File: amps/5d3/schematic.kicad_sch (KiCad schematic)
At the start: 43 parts, among them T2 PP : 8

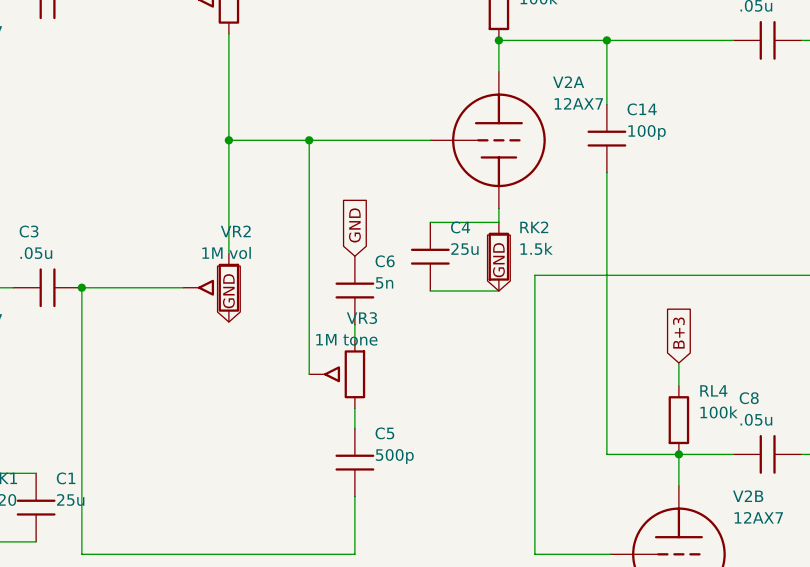
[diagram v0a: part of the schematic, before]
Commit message: Fix: one lettering convention per surface, engine-enforced; legend inside the viewBox
WS3 — layout pipeline + cross-surface value-consistency engine.

## One convention per surface (docs/lettering-conventions.md, new)

The same part stated its value in several notations at once. 5E3 C6 and 5D3 C6
rendered "5n" on the schematic, "0.005 µF · 600 V" in the parts list and
"0.005 µF" on the board. 5F6-A RD1 printed "4,700 Ω" beside neighbours printing
"15 kΩ". check_value_consistency proves the surfaces name the same QUANTITY; it
cannot see that they name it three ways. So each surface now has exactly one
convention and every one of them is gated:

* house units in bom.yaml/prose — engineering prefix with the mantissa 1…999,
  pF below 1000 pF and µF at and above it, no comma-grouped thousands. 19 values
  normalised (5E6-A, 5F6-A, 5F10, 6161, 6G2, 6G5, 6G6-B).
* schematic drafting shorthand — the unit letter is the SI prefix of the house
  unit, in the amp's declared idiom (meta.yaml conventions.notation: us|uk).
  British RKM/nanofarad practice on the Hiwatt and the 2204 is DECLARED, not
  normalised away; it is what those source drawings letter. Secondary ratings
  are space-separated fields with their own unit ("20u 600V"), never the era's
  dashed shorthand and never the house middot. 30 symbol values corrected across
  ten draw scripts.
* era sheet lettering — generated only, by era_pair(); documented cases and a
  corpus round-trip sweep in test_era_values.py, now 57 cases.

## Era-lettering fall-throughs closed

A value era_pair() refuses came back as the house string, and a house string can
be a whole sentence. Fixed at the source rather than per case:

* body_value() — a parenthetical GLOSS is never lettered on a component body.
  "selenium (silicon diode in modern builds)" was lettered in full on the 5E4-A
  and ran off the left edge of the page.
* twin cans letter as the era sheets did: 25 µF + 25 µF -> "25/25MFD".
* a repeat count is not a rating: "(×2)" com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
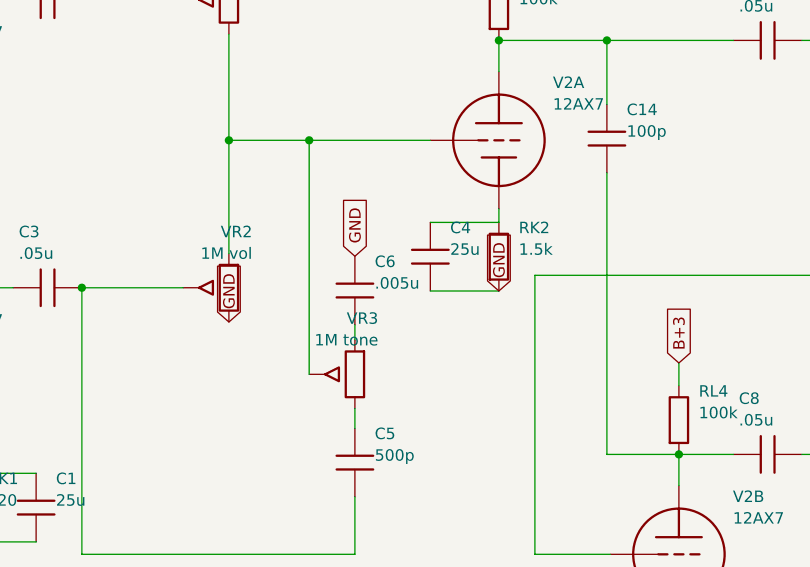
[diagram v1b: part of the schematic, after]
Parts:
- C6: value 5n -> .005u
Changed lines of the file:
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@@
     (in_bom yes) (on_board yes)
     (property "Reference" "C6" (at 106.2 117.49 0) (effects (font (size 1.27 1.27)) (justify left)))
-    (property "Value" "5n" (at 106.2 119.89 0) (effects (font (size 1.27 1.27)) (justify left))))
+    (property "Value" ".005u" (at 106.2 119.89 0) (effects (font (size 1.27 1.27)) (justify left))))
   (global_label "GND" (shape input) (at 104 116.88 270)
     (effects (font (size 1.27 1.27)) (justify left)))

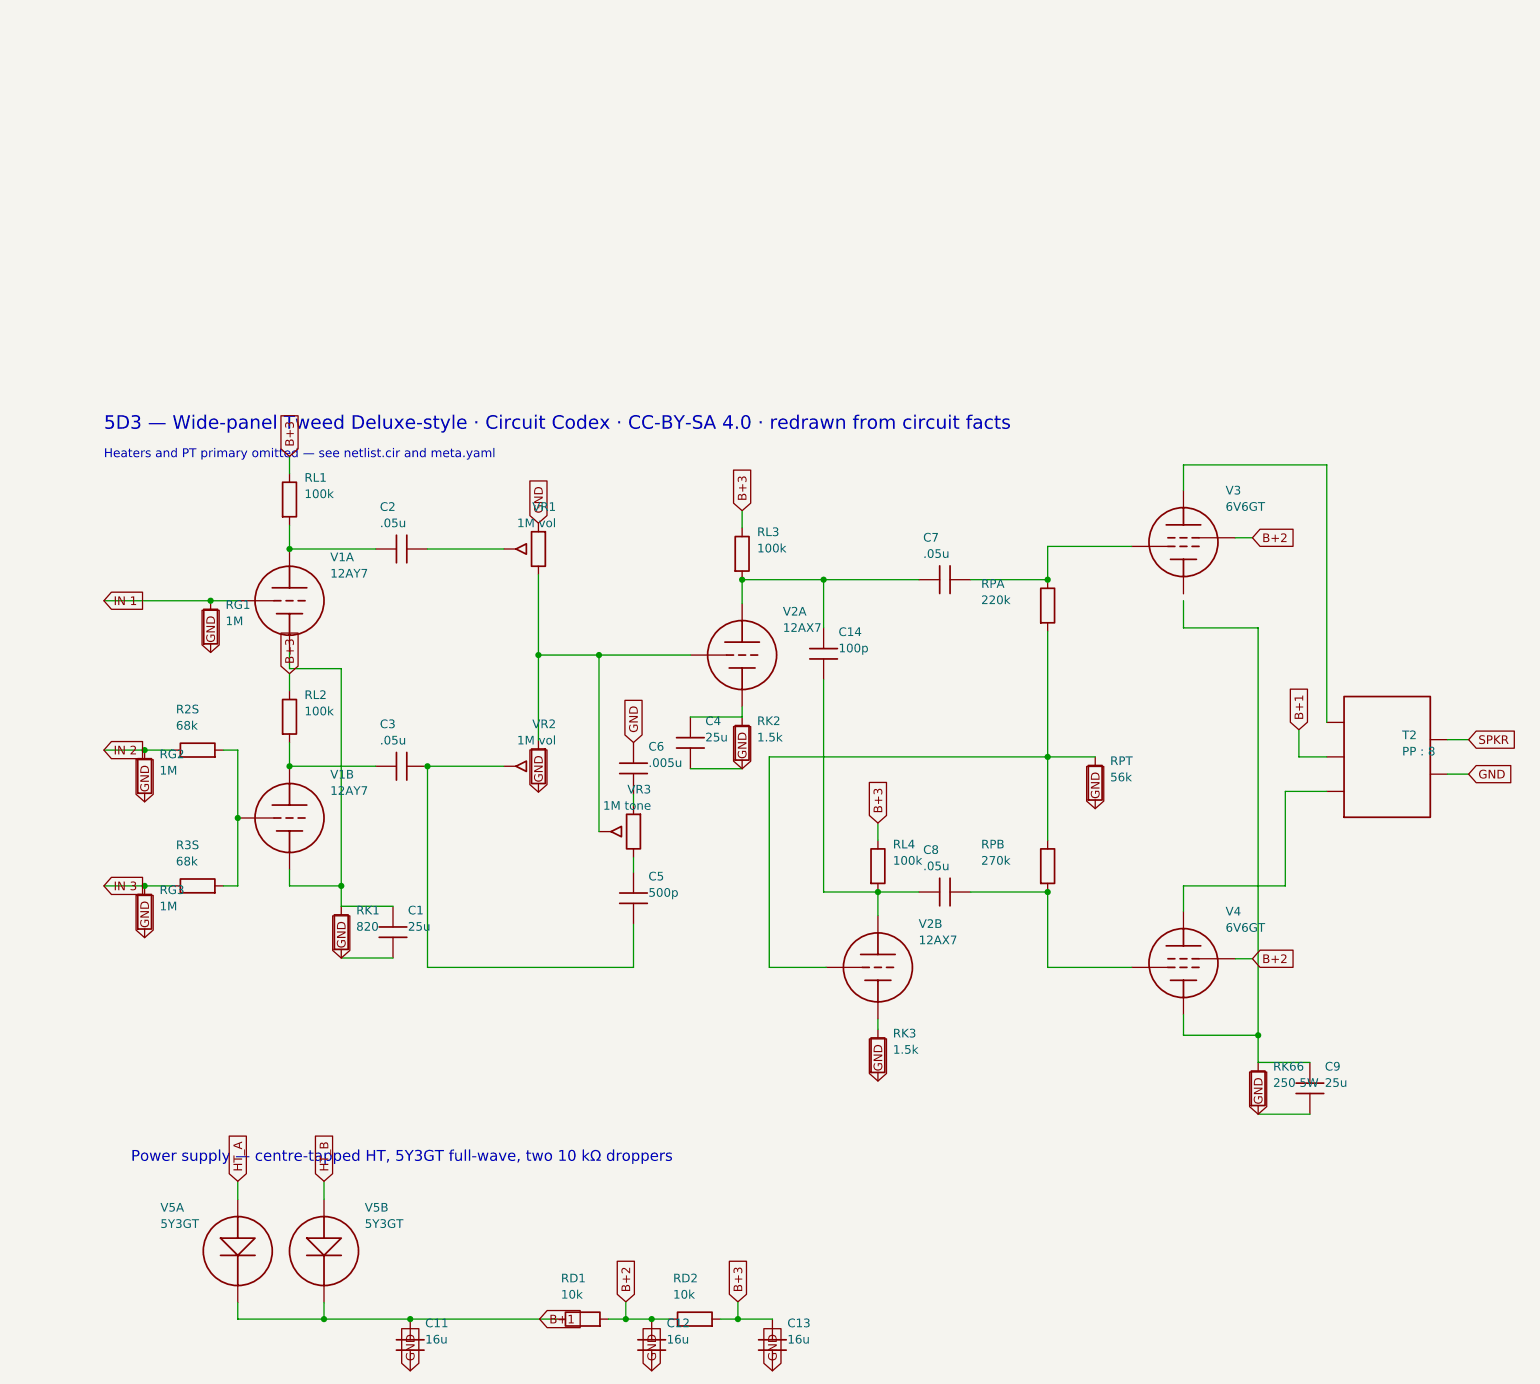
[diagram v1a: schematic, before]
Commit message: Update: regenerate every drawing the four merged units changed
The four parallel units all rewrote generators, so their committed artifacts
were each generated against only their own third of the merged pipeline. Every
schematic, both layout styles, the social cards and the manifest are rebuilt
here from the merged sources, so what ships is what the merged generators draw.

One integration fault the rebuild exposed, invisible to any single unit:

- 5E5-A: the note explaining that the Presence wiper and the 100k feedback
  resistor land on V3A's GRID (not its cathode, as on the 5F4) was added as a
  hand-placed `s.text()` at a coordinate chosen before the sheet gained a
  reserved notes band. Merged, it printed through the -32V bias label. Moved to
  `note()`, which wraps prose into that band — the exact failure mode the band
  was built to end.

Three conflicts resolved against docs/lettering-conventions.md rather than by
picking a side, since two units had corrected the same lines for different
reasons:

- 5E5-A tone/feedback caps take the corrected designators (C7, C8, C9, RNF —
  `C_tr1`/`C_NFB` were generator identifiers that had leaked onto a published
  board) with the house-derived lettering (`.01u 400V`, `500p`, `.1u 200V`).
  Dropping the working voltage or writing `.0005u` would have lost a rating the
  source prints and re-broken the pF/µF decade rule.
- 5D3 C6 and 6G6-B's three cathode resistors take the SI-prefix form the
  convention binds (`.005u`, `2.7k`, `1.5k`), keeping the ground-flag direction
  fix and the removal of the second `gnd()` that shorted each cathode it biased.
- 5F6-A's bias supply keeps both 8 µF cans drawn — the second was previously a
  parenthetical claiming one of two was shown — at the coordinates that clear
  the title-block strip.

All gates green, including check_value_consistency at zero disagreements.

🤖 Generated with [Claude Code](https://claude.com/claude-code)

Co-Authored-By: Claude Fable 5 <noreply@anthropic.com>
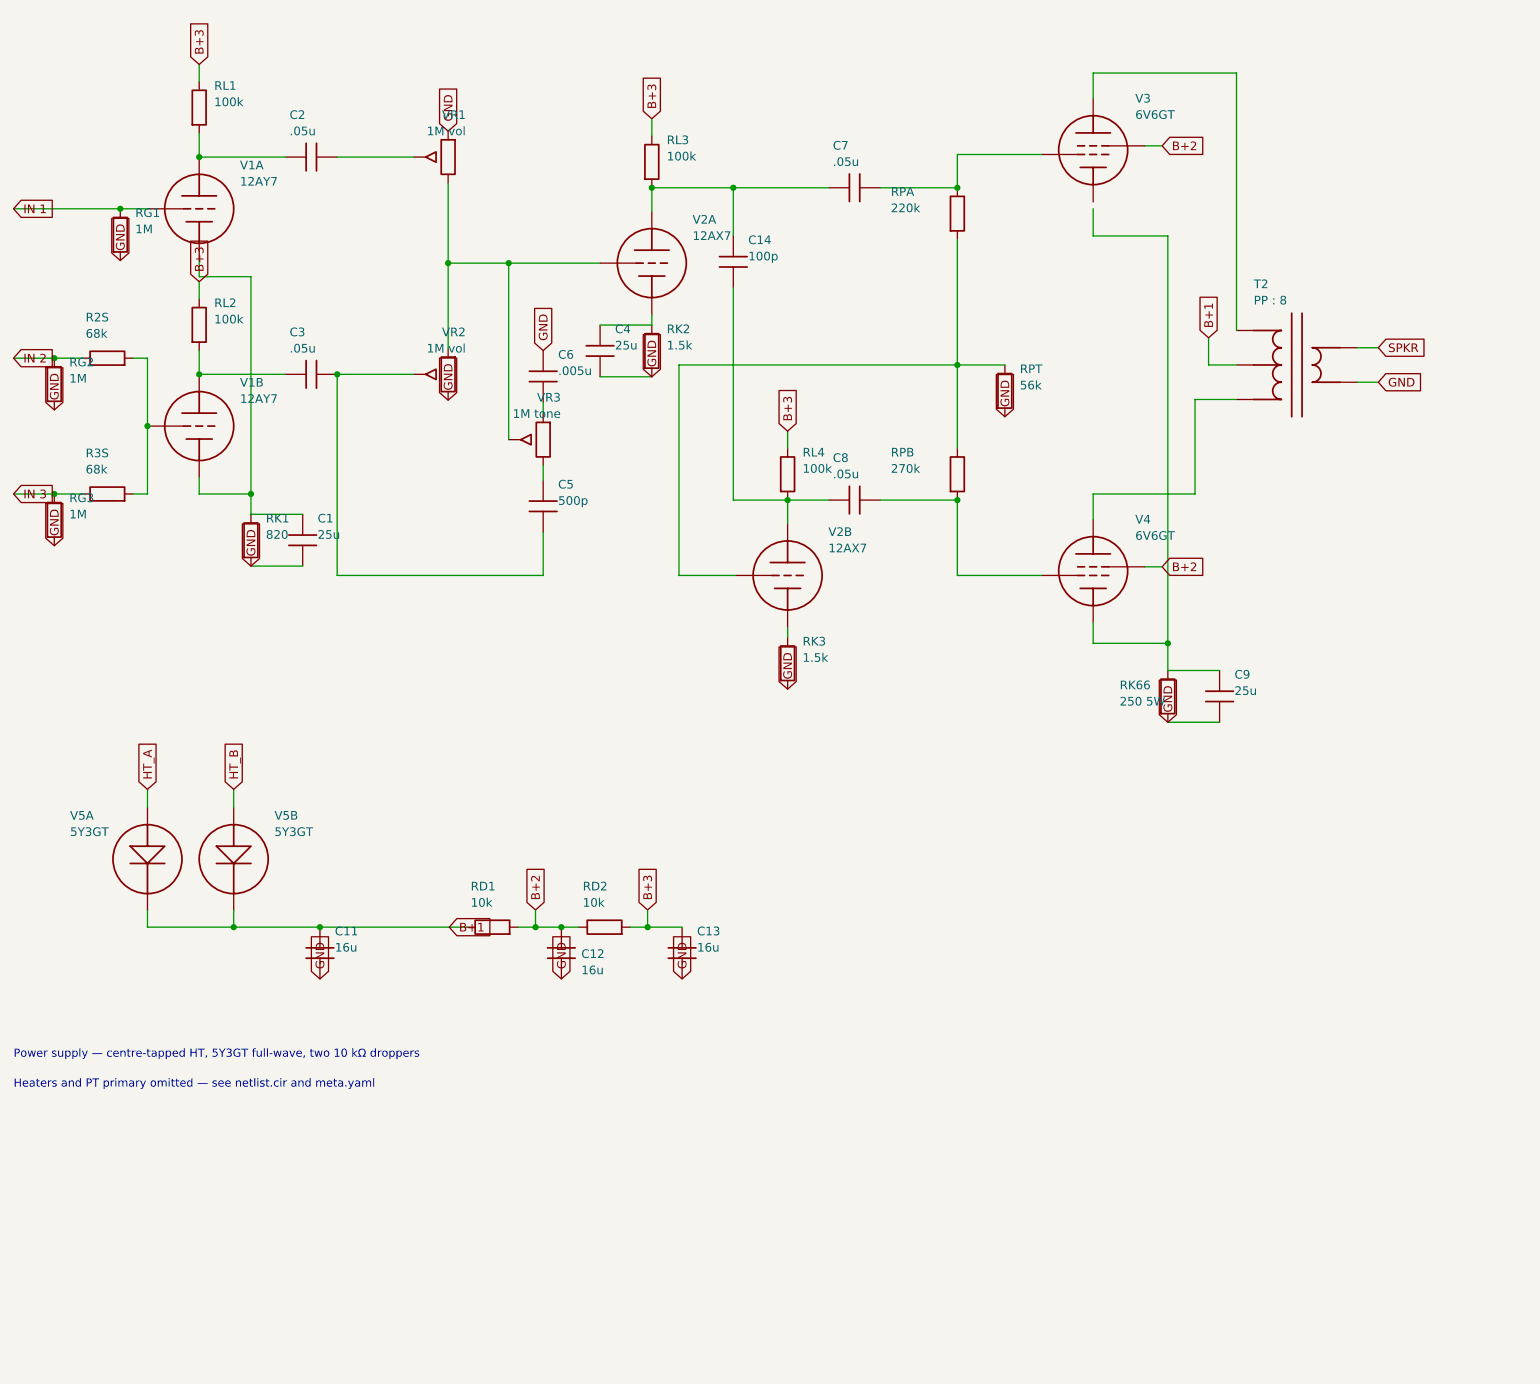
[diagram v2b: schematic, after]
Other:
- note removed: "5D3 — Wide-panel Tweed Deluxe-style · Circuit Codex · CC-BY-SA 4.0 · redrawn from circuit facts"
- company: (none) -> Circuit Codex
- title: (none) -> 5D3 — Wide-panel Tweed Deluxe-style
